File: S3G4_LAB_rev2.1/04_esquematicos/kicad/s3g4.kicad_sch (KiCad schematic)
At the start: 0 parts

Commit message: S8: dibuja la cadena de CH1 en una hoja plana A2 con Konnect
89 piezas de CH1_PIEZAS_Y_REDES.md, redes CH1_* locales, etiquetas
globales del §1, huellas estándar y campos MPN/LCSC.

Co-Authored-By: Claude Opus 5.5 (1M context) <noreply@anthropic.com>
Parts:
- added C101: 20pF 2% C0G 250V, Capacitor_SMD:C_0603_1608Metric, symbol Device:C
- added C102: 15pF 2% C0G 250V, Capacitor_SMD:C_0805_2012Metric, symbol Device:C
- added C103: DNP, Capacitor_SMD:C_0603_1608Metric, symbol Device:C
- added C104: 1nF 1% C0G, Capacitor_SMD:C_0603_1608Metric, symbol Device:C
- added C105: 68pF 5% C0G, Capacitor_SMD:C_0603_1608Metric, symbol Device:C
- added C106: 1.2nF C0G 200V, Capacitor_SMD:C_1206_3216Metric, symbol Device:C
- added C107: ~8.7pF C0G 200V, Capacitor_SMD:C_1206_3216Metric, symbol Device:C
- added C108: 1.8nF C0G 50V, Capacitor_SMD:C_0603_1608Metric, symbol Device:C
- added C109, C112: 56pF C0G, Capacitor_SMD:C_0603_1608Metric, symbol Device:C
- added C110: 47pF C0G, Capacitor_SMD:C_0603_1608Metric, symbol Device:C
- added C111: 220pF C0G, Capacitor_SMD:C_0603_1608Metric, symbol Device:C
- added C113: 1pF C0G, Capacitor_SMD:C_0603_1608Metric, symbol Device:C
- added C114: 1uF, Capacitor_SMD:C_0603_1608Metric, symbol Device:C
- added C115: 470pF C0G, Capacitor_SMD:C_0603_1608Metric, symbol Device:C
- added C116, C117, C118, C119, C120, C121, C122, C123, C124: 100nF X7R 16V, Capacitor_SMD:C_0402_1005Metric, symbol Device:C
- added C125, C126: 10uF X5R 16V, Capacitor_SMD:C_0805_2012Metric, symbol Device:C
- added D101: BAV199, Package_TO_SOT_SMD:SOT-23, symbol Diode:BAV99
- added D102, D103: BAV99, Package_TO_SOT_SMD:SOT-23, symbol Diode:BAV99
- added D104: 1N4148W, Diode_SMD:D_SOD-123, symbol Diode:1N4148W
- added J101: BNC, symbol Connector:Conn_Coaxial
- added K101: TQ2SA-5V-Z, symbol Relay:G6H-2
- added Q101: 2N7002, Package_TO_SOT_SMD:SOT-23, symbol Transistor_FET:2N7002
- added R101, R102: 549k 0.1%, Resistor_SMD:R_1206_3216Metric, symbol Device:R
- added R103: 11.0k 0.1%, Resistor_SMD:R_0805_2012Metric, symbol Device:R
- added R104, R105: 49.9k, Resistor_SMD:R_1206_3216Metric, symbol Device:R
- added R106: 10M, Resistor_SMD:R_1206_3216Metric, symbol Device:R
- added R107: 10M 1%, Resistor_SMD:R_0603_1608Metric, symbol Device:R
- added R108, R109, R125, R126, R137, R138, R139: 1k, Resistor_SMD:R_0603_1608Metric, symbol Device:R
- added R110, R119, R122: 270, Resistor_SMD:R_0603_1608Metric, symbol Device:R
- added R111: 150 1%, Resistor_SMD:R_0603_1608Metric, symbol Device:R
- added R112: 49.9 1%, Resistor_SMD:R_0603_1608Metric, symbol Device:R
- added R113, R114, R143, R144: 49.9, Resistor_SMD:R_0603_1608Metric, symbol Device:R
- added R115: 12.4k 0.1%, Resistor_SMD:R_0402_1005Metric, symbol Device:R
- added R116: 100 0.1%, Resistor_SMD:R_0402_1005Metric, symbol Device:R
- added R117, R120: 470, Resistor_SMD:R_0603_1608Metric, symbol Device:R
- added R118: 1.00k 1%, Resistor_SMD:R_0603_1608Metric, symbol Device:R
- added R121: 2.2k, Resistor_SMD:R_0603_1608Metric, symbol Device:R
- added R123, R124: 1.1k, Resistor_SMD:R_0603_1608Metric, symbol Device:R
- added R127, R129, R130: 10.0k 1%, Resistor_SMD:R_0603_1608Metric, symbol Device:R
- added R128: 7.5k, Resistor_SMD:R_0603_1608Metric, symbol Device:R
- added R131: 5.1k, Resistor_SMD:R_0603_1608Metric, symbol Device:R
- added R132, R145: 68, Resistor_SMD:R_0603_1608Metric, symbol Device:R
- added R133, R134: 10k 1%, Resistor_SMD:R_0603_1608Metric, symbol Device:R
- added R135: 100, Resistor_SMD:R_0603_1608Metric, symbol Device:R
- added R136: 100k, Resistor_SMD:R_0603_1608Metric, symbol Device:R
- added R140, R141, R142: 3.3k, Resistor_SMD:R_0603_1608Metric, symbol Device:R
- added R146: 560, Resistor_SMD:R_0603_1608Metric, symbol Device:R
- added R147: 120, Resistor_SMD:R_0603_1608Metric, symbol Device:R
- added R148, R149: 10, Resistor_SMD:R_0603_1608Metric, symbol Device:R
- added SW101: SS23H37L6, symbol Switch:SW_DP3T
- added U101: OPA810IDBVR, Package_TO_SOT_SMD:SOT-23-5, symbol Amplifier_Operational:OPA810xDBV
- added U102: 74HC4051D, Package_SO:SOIC-16_3.9x9.9mm_P1.27mm, symbol 74xx:74HC4051
- added U103, U105: AD8039ARZ-REEL7, Package_SO:SOIC-8_3.9x4.9mm_P1.27mm, symbol Amplifier_Operational:LM6172
- added U106: OPA836IDBVR, Package_TO_SOT_SMD:SOT-23-6, symbol Amplifier_Operational:ADA4807-1
- added VC101: 2-6pF, symbol Device:C_Trim
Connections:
- new net +3V3: R133.1, R134.1
- new net +AFE_4V9: C116.1, C118.1, C120.1, C122.1, C125.1, D101.2 (A), U101.5 (V+), U102.16 (VCC), U103.8 (V+), U105.8 (V+)
- new net -AFE_4V9: C117.1, C119.1, C121.1, C123.1, C126.1, D101.1 (K), U101.2 (V-), U102.7 (VEE), U103.4 (V-), U105.4 (V-)
- new net AGND: C104.2, C105.2, C107.2, C110.2, C112.2, C114.2, C115.2, C116.2, C117.2, C118.2, C119.2, C120.2, C121.2, C122.2, C123.2, C124.2, C125.2, C126.2, J101.2 (Ext), R103.2, R106.2, R107.2, R114.2, R116.2, R119.2, R122.2, R141.2, R142.2, R144.2, R147.2, SW101.3, U102.2 (A6), U102.6 (~{E}), U102.8 (GND), U106.2 (V-)
- new net CH1_AC: C108.2, SW101.1
- new net CH1_ADC: C115.1, R132.2
- new net CH1_BNC: C101.1, C106.1, J101.1 (In), R101.1, R104.1
- new net CH1_BUF_INP: R108.2, U101.3 (+)
- new net CH1_BUF_OUT: R109.1, R137.1, U101.1, U101.4 (-), U102.13 (A0)
- new net CH1_CPL_A: R133.2, SW101.5
- new net CH1_CPL_B: R134.2, SW101.8
- new net CH1_CPL_COM: R107.1, R108.1, SW101.2
- new net CH1_DIV_MID: C101.2, C102.1, C103.1, R101.2, R102.1, VC101.1
- new net CH1_DRV_OUT: C113.1, R129.1, R132.1, U106.1
- new net CH1_EQ: C107.1, K101.9, R106.1
- new net CH1_F1_A: R123.2, R148.1
- new net CH1_F1_B: R124.2, R149.1
- new net CH1_F1_INP: C110.1, R149.2, U105.3 (+)
- new net CH1_F1_MID: C109.1, R124.1, R148.2
- new net CH1_F1_OUT: C109.2, R125.1, R138.1, U105.1, U105.2 (-)
- new net CH1_F2_INP: C112.1, R126.2, R139.2, U105.5 (+)
- new net CH1_F2_MID: C111.1, R125.2, R126.1, R138.2, R139.1
- new net CH1_FILT_OUT: C111.2, R127.1, U105.6 (-), U105.7
- new net CH1_G1_INN: D102.3 (K), R118.2, R119.1, R141.1, U103.2 (-)
- new net CH1_G1_INP: D102.1 (K), D102.2 (A), R117.2, U103.3 (+)
- new net CH1_G1_OUT: R118.1, R120.1, U103.1
- new net CH1_G2_INN: D103.3 (K), R122.1, R142.1, R145.2, U103.6 (-)
- new net CH1_G2_INP: D103.1 (K), D103.2 (A), R120.2, U103.5 (+)
- new net CH1_G2_OUT: R121.1, R123.1, U103.7
- new net CH1_K_COIL_N: D104.2 (A), K101.10, Q101.3 (D)
- new net CH1_K_CTRL: R135.1
- new net CH1_K_GATE: Q101.1 (G), R135.2, R136.1
- new net CH1_LAD1: R109.2, R110.1, R137.2, R140.1, U102.14 (A1)
- new net CH1_LAD2: R110.2, R111.1, R140.2, U102.15 (A2)
- new net CH1_LAD3: R111.2, R112.1, U102.12 (A3)
- new net CH1_LAD4: R112.2, R113.1, R143.1, U102.1 (A4)
- new net CH1_LAD5: R113.2, R114.1, R143.2, R144.1, U102.5 (A5)
- new net CH1_MUX_OUT: R117.1, U102.3 (A)
- new net CH1_OFFSET_DAC: R128.1
- new net CH1_RF2_MID: R121.2, R145.1
- new net CH1_ROFF_MID: R128.2, R146.1
- new net CH1_RS_MID: R104.2, R105.1
- new net CH1_SEL: C108.1, D101.3 (K), K101.3, SW101.4
- new net CH1_SENSEL_A: U102.11 (S0)
- new net CH1_SENSEL_B: U102.10 (S1)
- new net CH1_SENSEL_C: U102.9 (S2)
- new net CH1_SUM: C113.2, R127.2, R129.2, R146.2, U106.4 (-)
- new net CH1_TAP: C102.2, C103.2, C104.1, C105.1, K101.2, R102.2, R103.1, VC101.2
- new net CH1_VCHECK: R115.2, R116.1, U102.4 (A7)
- new net CH1_VMID: C114.1, R130.2, R131.1, U106.3 (+)
- new net CH1_VMID_LO: R131.2, R147.1
- new net CH1_X1: C106.2, K101.4, K101.8, R105.2
- new net GND: Q101.2 (S), R136.2, SW101.6
- new net RELAY_COM: D104.1 (K), K101.1
- new net VDDA: C124.1, U106.5 (~{DISABLE}), U106.6 (V+)
- new net VREF_2V5: R115.1, R130.1
- no-connect marks 0 -> 2

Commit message: S8: rótulos, notas del §5, campos legibles; netlist, ERC y verificar_s8.py
verificar_s8.py lee CH1_PIEZAS_Y_REDES.md y compara pin a pin con la
netlist exportada; sale con 0 (sin diferencias).

Co-Authored-By: Claude Opus 5.5 (1M context) <noreply@anthropic.com>
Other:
- note added: "1 · Entrada: J101, divisor ÷100, rama ×1 y réplica"
- note added: "2 · Relé K101 TQ2SA-5V-Z, reposo = ÷100"
- note added: "3 · Sujeción D101, acoplo SW101, C_AC, R_BIAS y R_PROT"
- note added: "4 · Buffer U101"
- note added: "5 · Escalera, VCHECK y U102"
- note added: "6 · Ganancia ×50 U103A ×5.016, U103B ×10.08, R_SER y BAV99"
- note added: "7 · Filtro anti-alias U105 (dos Sallen-Key)"
- note added: "8 · Etapa final U106, VMID y red del pin (CH1_ADC = PA0)"
- note added: "9 · Driver del relé (Q101, D104, R135, R136) La corriente de la bobina vuelve por GND, no por AGND."
- note added: "ABIERTO (§5 de CH1_PIEZAS_Y_REDES.md), no dibujado: - Circuito común del economizador (P-MOSFET de arranque, Schottky desde 3.3 V, línea RELAY_KICK): va en la hoja de control/alimentación, no en la de CH1. - Huella del TQ2SA: comprobarla contra la p. 11 de la hoja (vista superior, patrón SA). - TVS de riel: es de la hoja de alimentación, no de CH1. - El 74HC165 que lee CH1_CPL_A/B cuelga del STM3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"
- note added: "K101: símbolo provisional Relay:G6H-2, mismo pinout que el TQ2SA (ASCTB14E p. 10): bobina 1(+)/10, polo 1: 3 común, 2 NC, 4 NO; polo 2: 8 común, 9 NC, 7 NO. Pines 5 y 6 sin función. Huella sin asignar: comprobar con la p. 11."
- note added: "SW101: símbolo provisional (Switch:SW_DP3T). Los números de pin siguen CH1_PIEZAS_Y_REDES §2.3: común = 2 / 6; T1 = AC (1 / 5), T2 = GND (3 / 7), T3 = DC (4 / 8). El dibujo del símbolo no lo refleja. Patas MP ×4: sin conexión en el esquema (se decide en la placa)."

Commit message: S8: simbolos y huellas propios de CH1, DNP de C103 y C125/C126 a 25 V
- lib/gen/gen_ch1_parts.py genera las huellas del rele TQ2SA (SMD), el
  conmutador SS23H37, el BNC Kinghelm y el trimmer SEHWA, y los simbolos
  TQ2SA-5V-Z y SS23H37L6, con cotas de los planos y de la huella EasyEDA.
- Auditoria de Claude (AUDITORIA_CLAUDE_S8.md), paquete de S8 y BOM.
- Pinouts de 2N7002, BAV99 y 1N4148W verificados con sus hojas.

Co-Authored-By: Claude Opus 5.5 <noreply@anthropic.com>
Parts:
- C103: now not fitted
- C125, C126: value 10uF X5R 16V -> 10uF X5R 25V

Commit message: S8b: CH1 redibujado con cables, uniones y símbolos de alimentación
Símbolos propios de K101 (s3g4:TQ2SA-5V-Z) y SW101 (s3g4:SS23H37L6),
huellas propias de J101 y VC101. Mismas redes: verificar_s8.py da 0.

Co-Authored-By: Claude Opus 5.5 <noreply@anthropic.com>
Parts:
- removed K101: TQ2SA-5V-Z, symbol Relay:G6H-2
- removed SW101: SS23H37L6, symbol Switch:SW_DP3T
- added K101: TQ2SA-5V-Z, s3g4:Relay_Panasonic_TQ2SA_SMD, symbol s3g4:TQ2SA-5V-Z
- added SW101: SS23H37L6, s3g4:SW_Slide_DP3T_XKB_SS23H37, symbol s3g4:SS23H37L6
- C103: Nota DNP (hueco de seguro, DECISIONS 4 oct). Atributo DNP de KiC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 -> DNP (hueco de seguro, DECISIONS 4 oct)
- J101: footprint (none) -> s3g4:BNC_Kinghelm_KH-BNC50-3511_Horizontal; Nota Símbolo provisional: Connector:Conn_Coaxial (centro 1, cuer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 -> (none)
- VC101: footprint (none) -> s3g4:C_Trimmer_SEHWA_STC3MA06_3.2x4.5mm; Nota Símbolo provisional: Device:C_Trim -> (none)
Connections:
- net AGND: now also C110.1, C112.1, C114.1, R119.1, R122.1, R141.1, R142.1, SW101.3 (T2); no longer C110.2, C112.2, C114.2, R119.2, R122.2, R141.2, R142.2
- net CH1_AC: now also SW101.1 (T1)
- net CH1_CPL_A: now also SW101.5 (T1)
- net CH1_CPL_B: now also SW101.8 (T3)
- net CH1_CPL_COM: now also SW101.2 (COM)
- net CH1_DRV_OUT: now also C113.2, R129.2; no longer C113.1, R129.1
- net CH1_EQ: now also K101.9 (NC)
- net CH1_F1_INP: now also C110.2; no longer C110.1
- net CH1_F2_INP: now also C112.2; no longer C112.1
- net CH1_G1_INN: now also R118.1, R119.2, R141.2; no longer R118.2, R119.1, R141.1
- net CH1_G1_OUT: now also R118.2; no longer R118.1
- net CH1_G2_INN: now also R122.2, R142.2, R145.1; no longer R122.1, R142.1, R145.2
- net CH1_G2_OUT: now also R121.2; no longer R121.1
- net CH1_K_COIL_N: now also K101.10 (-)
- net CH1_K_GATE: now also R136.2; no longer R136.1
- net CH1_RF2_MID: now also R121.1, R145.2; no longer R121.2, R145.1
- net CH1_SEL: now also K101.3 (COM), SW101.4 (T3)
- net CH1_SUM: now also C113.1, R129.1; no longer C113.2, R129.2
- net CH1_TAP: now also K101.2 (NC)
- net CH1_VMID: now also C114.2; no longer C114.1
- net CH1_X1: now also K101.4 (NO), K101.8 (COM)
- net GND: now also R136.1, SW101.6 (COM); no longer R136.2
- net RELAY_COM: now also K101.1 (+)
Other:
- note removed: "1 · Entrada: J101, divisor ÷100, rama ×1 y réplica"
- note removed: "2 · Relé K101 TQ2SA-5V-Z, reposo = ÷100"
- note removed: "3 · Sujeción D101, acoplo SW101, C_AC, R_BIAS y R_PROT"
- note removed: "4 · Buffer U101"
- note removed: "5 · Escalera, VCHECK y U102"
- note removed: "6 · Ganancia ×50 U103A ×5.016, U103B ×10.08, R_SER y BAV99"
- note removed: "7 · Filtro anti-alias U105 (dos Sallen-Key)"
- note removed: "8 · Etapa final U106, VMID y red del pin (CH1_ADC = PA0)"
- note removed: "9 · Driver del relé (Q101, D104, R135, R136) La corriente de la bobina vuelve por GND, no por AGND."
- note removed: "ABIERTO (§5 de CH1_PIEZAS_Y_REDES.md), no dibujado: - Circuito común del economizador (P-MOSFET de arranque, Schottky desde 3.3 V, línea RELAY_KICK): va en la hoja de control/alimentación, no en la de CH1. - Huella del TQ2SA: comprobarla contra la p. 11 de la hoja (vista superior, patrón SA). - TVS de riel: es de la hoja de alimentación, no de CH1. - El 74HC165 que lee CH1_CPL_A/B cuelga del STM3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"
- note removed: "K101: símbolo provisional Relay:G6H-2, mismo pinout que el TQ2SA (ASCTB14E p. 10): bobina 1(+)/10, polo 1: 3 común, 2 NC, 4 NO; polo 2: 8 común, 9 NC, 7 NO. Pines 5 y 6 sin función. Huella sin asignar: comprobar con la p. 11."
- note removed: "SW101: símbolo provisional (Switch:SW_DP3T). Los números de pin siguen CH1_PIEZAS_Y_REDES §2.3: común = 2 / 6; T1 = AC (1 / 5), T2 = GND (3 / 7), T3 = DC (4 / 8). El dibujo del símbolo no lo refleja. Patas MP ×4: sin conexión en el esquema (se decide en la placa)."
- moved on the sheet: C101, C102, C103, C104, C105, C106, C107, C108, C109, C110, C111, C112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

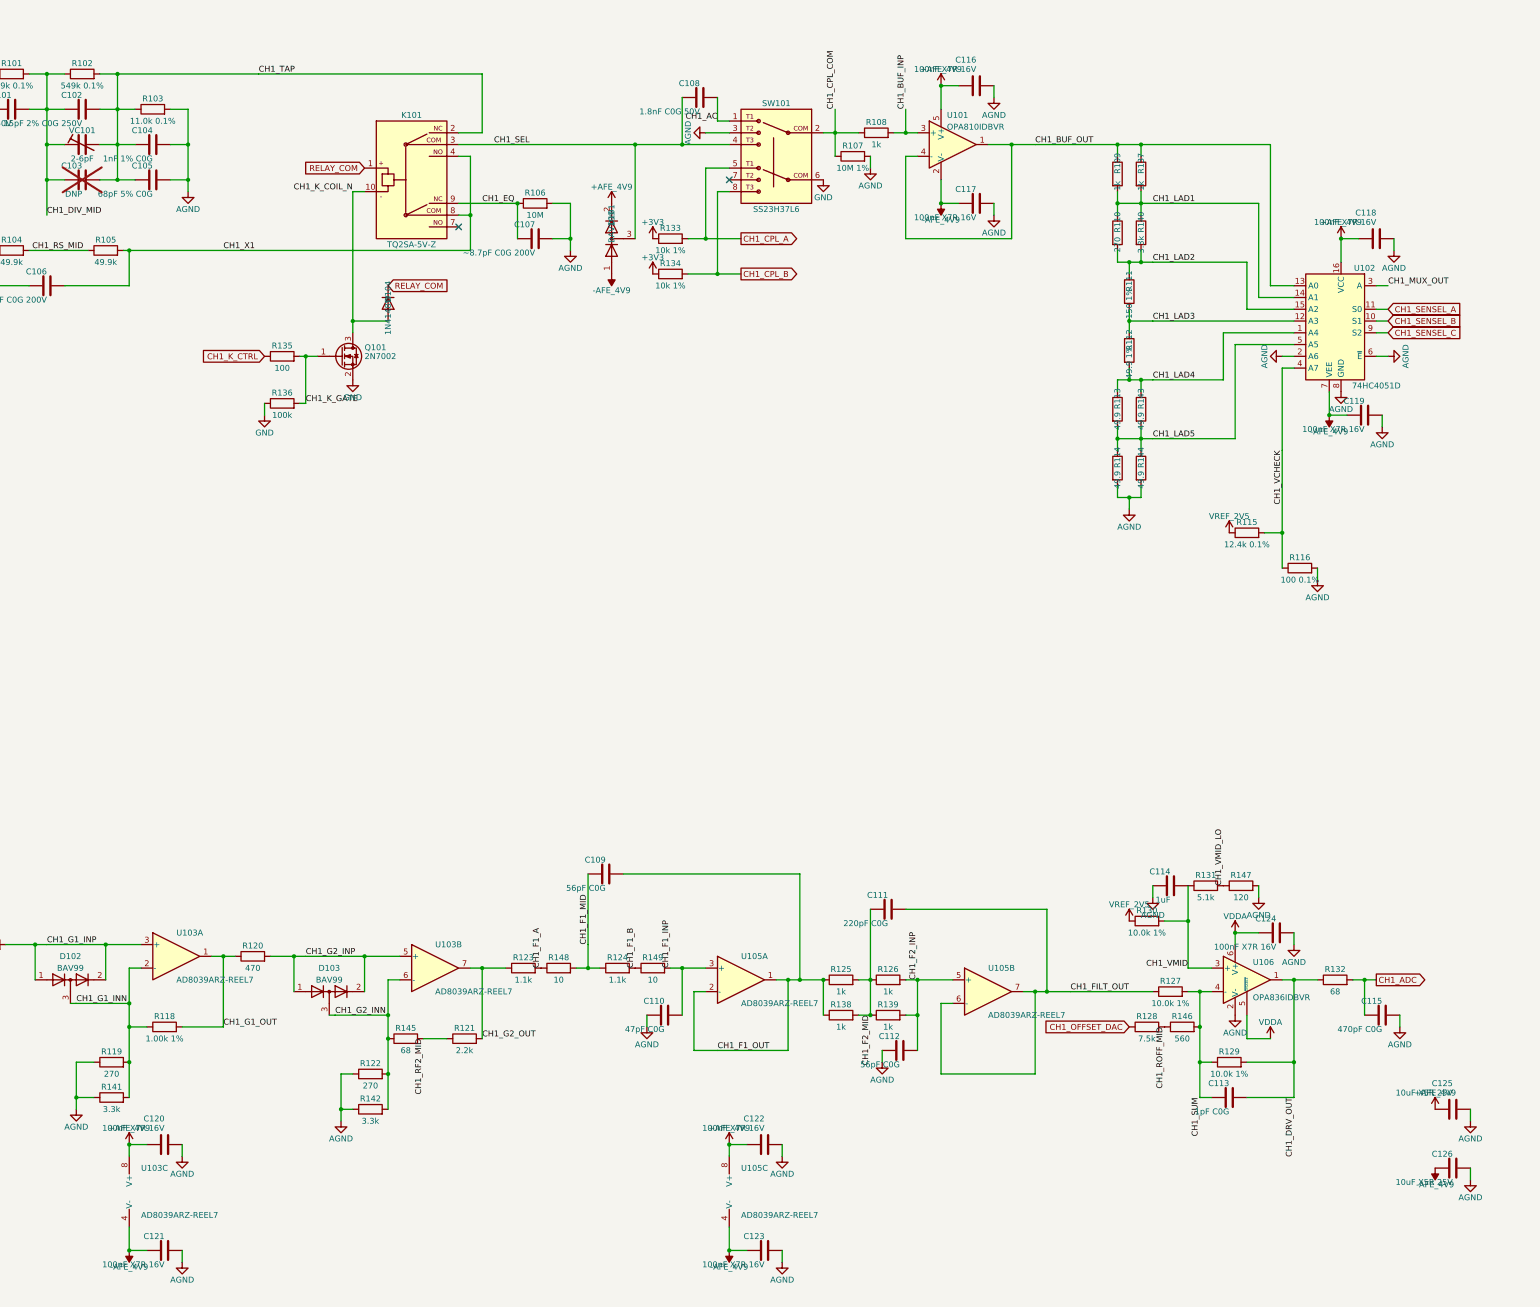
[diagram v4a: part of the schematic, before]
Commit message: S8b: desacoplos verticales junto a su CI y etapa final reordenada para que no se pisen textos
verificar_s8.py sale con 0; ERC igual que antes (15).

Co-Authored-By: Claude Opus 5.5 <noreply@anthropic.com>
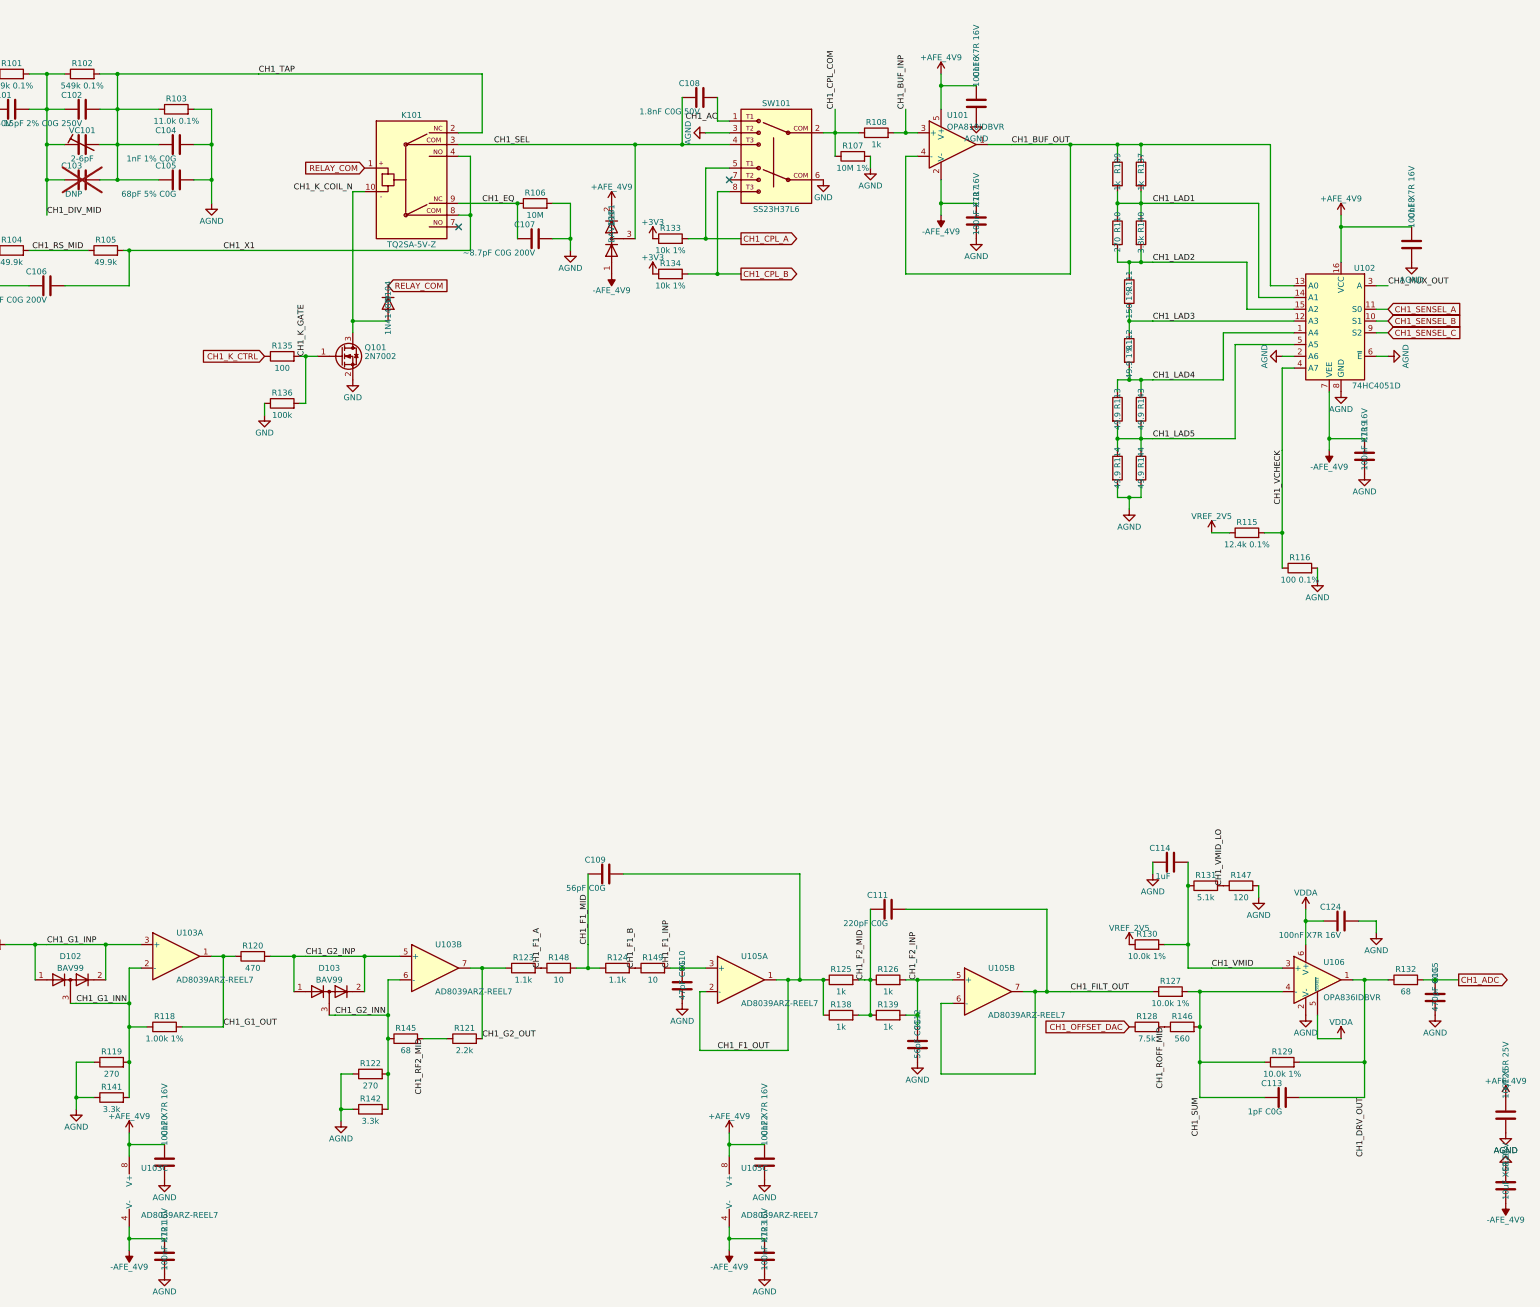
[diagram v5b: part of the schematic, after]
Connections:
- net -AFE_4V9: now also C126.2; no longer C126.1
- net AGND: now also C110.2, C112.2, C126.1; no longer C110.1, C112.1, C126.2
- net CH1_F1_INP: now also C110.1; no longer C110.2
- net CH1_F2_INP: now also C112.1; no longer C112.2
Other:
- moved on the sheet: C104, C105, C110, C112, C113, C114, C115, C116, C117, C118, C119, C120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

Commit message: S8b: rotulos de bloque, texto de CH1 y valores de pasivos reubicados para que no se pisen
Co-Authored-By: Claude Sonnet 5.5 <noreply@anthropic.com>
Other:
- note added: "1 · Entrada: J101, divisor ÷100, rama ×1 y réplica"
- note added: "2 · Relé K101 TQ2SA-5V-Z, reposo = ÷100"
- note added: "3 · Sujeción D101, acoplo SW101, C_AC, R_BIAS y R_PROT"
- note added: "4 · Buffer U101"
- note added: "5 · Escalera, VCHECK y U102"
- note added: "6 · Ganancia ×50 U103A ×5.016, U103B ×10.08, R_SER y BAV99"
- note added: "7 · Filtro anti-alias U105 (dos Sallen-Key)"
- note added: "8 · Etapa final U106, VMID y red del pin (CH1_ADC = PA0)"
- note added: "9 · Driver del relé (Q101, D104, R135, R136) La corriente de la bobina vuelve por GND, no por AGND."
- note added: "ABIERTO (§5 de CH1_PIEZAS_Y_REDES.md), no dibujado: - Circuito común del economizador (P-MOSFET de arranque, Schottky desde 3.3 V, línea RELAY_KICK): va en la hoja de control/alimentación, no en la de CH1. - TVS de riel: es de la hoja de alimentación, no de CH1. - El 74HC165 que lee CH1_CPL_A/B cuelga del STM32, en el bus de los 74HCT595. - Partición AGND/GND: la decide Keneth al hacer la placa; 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"
